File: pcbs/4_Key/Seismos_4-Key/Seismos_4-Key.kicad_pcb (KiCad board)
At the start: 2 copper layers, 19 x 86.4 mm, 9 parts, among them J1 SM09B-SRSS-TB(LF)(SN), SW1 Switch_SK6812-E_Diode, SW2 Switch_SK6812-E_Diode, SW3 Switch_SK6812-E_Diode, SW4 Switch_SK6812-E_Diode

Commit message: Update 4Key Column STEP
Wrong footprint definitions resulted in no parts shown so fixed it
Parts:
- SW1, SW2, SW3, SW4: footprint Seismos-lib:Switch_SK6812-E_Diode -> Seismos-libs:Switch_SK6812-E_Diode
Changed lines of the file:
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@@
   (net 15 "/V+")
   (net 16 "/RGB_Out")
-  (footprint "Seismos-lib:Switch_SK6812-E_Diode" (layer "F.Cu")
+  (footprint "Seismos-libs:Switch_SK6812-E_Diode" (layer "F.Cu")
     (at 47 60)
     (property "Sheetfile" "Seismos_4-Key.kicad_sch")
@@
     (fp_arc (start -4.3 3.85) (mid -4.113909 3.450736) (end -3.7 3.3)
       (stroke (width 0.15) (type solid)) (layer "B.SilkS"))
-    (fp_arc (start 2.299999 1.499999) (mid 1.672792 2.814212) (end 0.3 3.3)
+    (fp_arc (start 2.299999 1.499999) (mid 1.672792 2.814213) (end 0.3 3.3)
       (stroke (width 0.15) (type solid)) (layer "B.SilkS"))
     (fp_arc (start 2.3 1.35) (mid 2.361091 1.002513) (end 2.65 0.8)
@@
     (pad "MX2" smd rect (at 6.86 2.54) (size 2.4 2.6) (layers "B.Cu" "B.Paste" "B.Mask")
       (net 14 "/Col_In") (pinfunction "P0") (pintype "bidirectional") (solder_mask_margin 0.0635))
-    (model "/share/KiCad Projects/libs/Seismos-libs/LED_SK6812MINI-E.step"
+    (model "${KIPRJMOD}/../../../libs/Seismos-libs/LED_SK6812MINI-E.step"
       (offset (xyz -0.142 9.588 0))
       (scale (xyz 1 1 1))
       (rotate (xyz 0 0 0))
     )
-    (model "/share/KiCad Projects/libs/Seismos-libs/PG1350-socket.STEP"
+    (model "${KIPRJMOD}/../../../libs/Seismos-libs/PG1350-socket.STEP"
       (offset (xyz 5.008 -3.812 -1.7))
       (scale (xyz 1 1 1))
@@
     )
   )
-  (footprint "Seismos-lib:Switch_SK6812-E_Diode" (layer "F.Cu")
+  (footprint "Seismos-libs:Switch_SK6812-E_Diode" (layer "F.Cu")
     (at 47 41)
     (property "Sheetfile" "Seismos_4-Key.kicad_sch")
@@
         (effects (font (size 1 1) (thickness 0.15)) (justify mirror))
     )
+    (fp_text user "${REFERENCE}" (at -0.142 2.612 unlocked) (layer "F.Fab")
+        (effects (font (size 1 1) (thickness 0.15)))
+    )
     (fp_text user "${REFERENCE}" (at -0.142 -4.46 unlocked) (layer "F.Fab")
         (effects (font (size 1 1) (thickness 0.15)))
     )
-    (fp_text user "${REFERENCE}" (at -0.142 2.612 unlocked) (layer "F.Fab")
-        (effects (font (size 1 1) (thickness 0.15)))
-    )
     (fp_line (start -7.25 1.45) (end -7.25 6.35)
       (stroke (width 0.15) (type solid)) (layer "B.SilkS"))
@@
     (fp_arc (start -4.3 3.85) (mid -4.113909 3.450736) (end -3.7 3.3)
       (stroke (width 0.15) (type solid)) (layer "B.SilkS"))
-    (fp_arc (start 2.299999 1.499999) (mid 1.672792 2.814212) (end 0.3 3.3)
+    (fp_arc (start 2.299999 1.499999) (mid 1.672792 2.814213) (end 0.3 3.3)
       (stroke (width 0.15) (type solid)) (layer "B.SilkS"))
     (fp_arc (start 2.3 1.35) (mid 2.361091 1.002513) (end 2.65 0.8)
@@
     (pad "MX2" smd rect (at 6.86 2.54) (size 2.4 2.6) (layers "B.Cu" "B.Paste" "B.Mask")
       (net 14 "/Col_In") (pinfunction "P0") (pintype "bidirectional") (solder_mask_margin 0.0635))
-    (model "/share/KiCad Projects/libs/Seismos-libs/LED_SK6812MINI-E.step"
+    (model "${KIPRJMOD}/../../../libs/Seismos-libs/LED_SK6812MINI-E.step"
       (offset (xyz -0.142 9.588 0))
       (scale (xyz 1 1 1))
       (rotate (xyz 0 0 0))
     )
-    (model "/share/KiCad Projects/libs/Seismos-libs/PG1350-socket.STEP"
+    (model "${KIPRJMOD}/../../../libs/Seismos-libs/PG1350-socket.STEP"
       (offset (xyz 5.008 -3.812 -1.7))
       (scale (xyz 1 1 1))
@@
     )
   )
-  (footprint "Seismos-lib:Switch_SK6812-E_Diode" (layer "F.Cu")
+  (footprint "Seismos-libs:Switch_SK6812-E_Diode" (layer "F.Cu")
     (at 47 79)
     (property "Sheetfile" "Seismos_4-Key.kicad_sch")
@@
         (effects (font (size 1 1) (thickness 0.15)) (justify mirror))
     )
+    (fp_text user "${REFERENCE}" (at -0.142 2.612 unlocked) (layer "F.Fab")
+        (effects (font (size 1 1) (thickness 0.15)))
+    )
     (fp_text user "${REFERENCE}" (at -0.142 -4.46 unlocked) (layer "F.Fab")
         (effects (font (size 1 1) (thickness 0.15)))
     )
-    (fp_text user "${REFERENCE}" (at -0.142 2.612 unlocked) (layer "F.Fab")
-        (effects (font (size 1 1) (thickness 0.15)))
-    )
     (fp_line (start -7.25 1.45) (end -7.25 6.35)
       (stroke (width 0.15) (type solid)) (layer "B.SilkS"))
@@
     (fp_arc (start -4.3 3.85) (mid -4.113909 3.450736) (end -3.7 3.3)
       (stroke (width 0.15) (type solid)) (layer "B.SilkS"))
-    (fp_arc (start 2.299999 1.499999) (mid 1.672792 2.814212) (end 0.3 3.3)
+    (fp_arc (start 2.299999 1.499999) (mid 1.672792 2.814213) (end 0.3 3.3)
       (stroke (width 0.15) (type solid)) (layer "B.SilkS"))
     (fp_arc (start 2.3 1.35) (mid 2.361091 1.002513) (end 2.65 0.8)
@@
     (pad "MX2" smd rect (at 6.86 2.54) (size 2.4 2.6) (layers "B.Cu" "B.Paste" "B.Mask")
       (net 14 "/Col_In") (pinfunction "P0") (pintype "bidirectional") (solder_mask_margin 0.0635))
-    (model "/share/KiCad Projects/libs/Seismos-libs/LED_SK6812MINI-E.step"
+    (model "${KIPRJMOD}/../../../libs/Seismos-libs/LED_SK6812MINI-E.step"
       (offset (xyz -0.142 9.588 0))
       (scale (xyz 1 1 1))
       (rotate (xyz 0 0 0))
     )
-    (model "/share/KiCad Projects/libs/Seismos-libs/PG1350-socket.STEP"
+    (model "${KIPRJMOD}/../../../libs/Seismos-libs/PG1350-socket.STEP"
       (offset (xyz 5.008 -3.812 -1.7))
       (scale (xyz 1 1 1))
@@
     )
   )
-  (footprint "Seismos-lib:Switch_SK6812-E_Diode" (layer "F.Cu")
+  (footprint "Seismos-libs:Switch_SK6812-E_Diode" (layer "F.Cu")
     (at 47 98)
     (property "Sheetfile" "Seismos_4-Key.kicad_sch")
@@
     (fp_arc (start -4.3 3.85) (mid -4.113909 3.450736) (end -3.7 3.3)
       (stroke (width 0.15) (type solid)) (layer "B.SilkS"))
-    (fp_arc (start 2.299999 1.499999) (mid 1.672792 2.814212) (end 0.3 3.3)
+    (fp_arc (start 2.299999 1.499999) (mid 1.672792 2.814213) (end 0.3 3.3)
       (stroke (width 0.15) (type solid)) (layer "B.SilkS"))
     (fp_arc (start 2.3 1.35) (mid 2.361091 1.002513) (end 2.65 0.8)
@@
     (pad "MX2" smd rect (at 6.86 2.54) (size 2.4 2.6) (layers "B.Cu" "B.Paste" "B.Mask")
       (net 14 "/Col_In") (pinfunction "P0") (pintype "bidirectional") (solder_mask_margin 0.0635))
-    (model "/share/KiCad Projects/libs/Seismos-libs/LED_SK6812MINI-E.step"
+    (model "${KIPRJMOD}/../../../libs/Seismos-libs/LED_SK6812MINI-E.step"
       (offset (xyz -0.142 9.588 0))
       (scale (xyz 1 1 1))
       (rotate (xyz 0 0 0))
     )
-    (model "/share/KiCad Projects/libs/Seismos-libs/PG1350-socket.STEP"
+    (model "${KIPRJMOD}/../../../libs/Seismos-libs/PG1350-socket.STEP"
       (offset (xyz 5.008 -3.812 -1.7))
       (scale (xyz 1 1 1))
@@
     (pad "S2" smd rect (at 5.3 0 270) (size 1.8 1.2) (layers "F.Cu" "F.Paste" "F.Mask")
       (net 6 "GND") (pinfunction "SHIELD") (pintype "passive"))
-    (model "/share/KiCad Projects/libs/Seismos-libs/SM09B-SRSS-TB_LF__SN_.step"
+    (model "${KIPRJMOD}/../../../libs/Seismos-libs/SM09B-SRSS-TB_LF__SN_.step"
       (offset (xyz -2 3.3 -0.4))
       (scale (xyz 1 1 1))
@@
         (xy 57.125 111.925)
         (xy 56.825 24.525)
-        (xy 37.35 24.95)
-      )
-    )
+      )
+    )

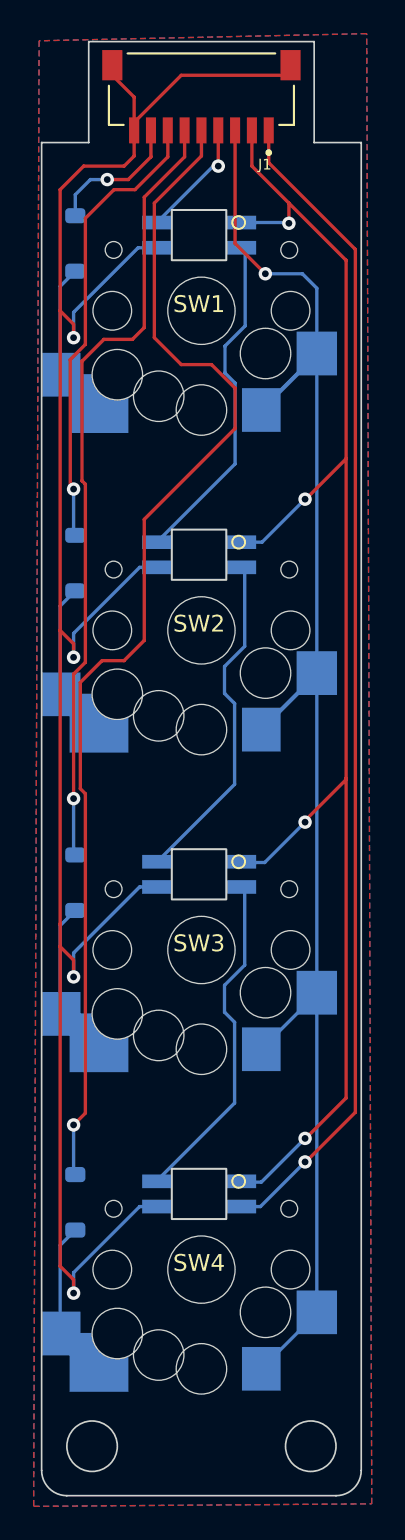
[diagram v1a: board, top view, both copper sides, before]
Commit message: Fix footprint errors and new 2x2 PCB
Fixed keyboard_reversible.pretty not being included.
Added a 2x2 PCB for the thumb.

Added a note regarding DRC errors involving two specific footprints...
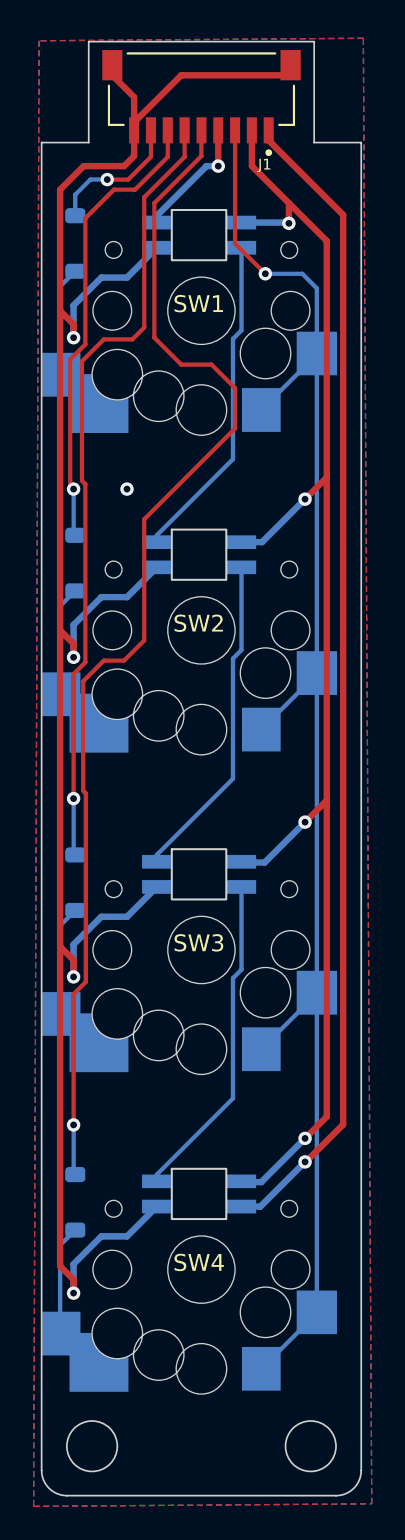
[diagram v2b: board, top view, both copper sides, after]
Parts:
- added G***: LOGO, Seismos-libs:ReSummit_Logo, B.Cu at (47.0, 30.0)
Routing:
- net /V+: track 88.2 -> 83.8 mm
- net Net-(SW1B-DOUT): track 20.7 -> 19.6 mm
- net /RGB_In: track 6.57 -> 7.70 mm
- net Net-(SW3B-DOUT): track 20.3 -> 19.6 mm
- net Net-(SW2B-DOUT): track 20.3 -> 19.6 mm
- net /RGB_Out: track 69.0 -> 68.4 mm
- net GND: track 125.9 -> 126.4 mm, vias 4 -> 5
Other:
- board text added: "Designed by ReSummit"
